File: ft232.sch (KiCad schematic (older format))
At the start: 18 parts, among them J1 USB_B, U7 FT232RL, U8 PS2911-1-F3-A, U9 PS2911-1-F3-A

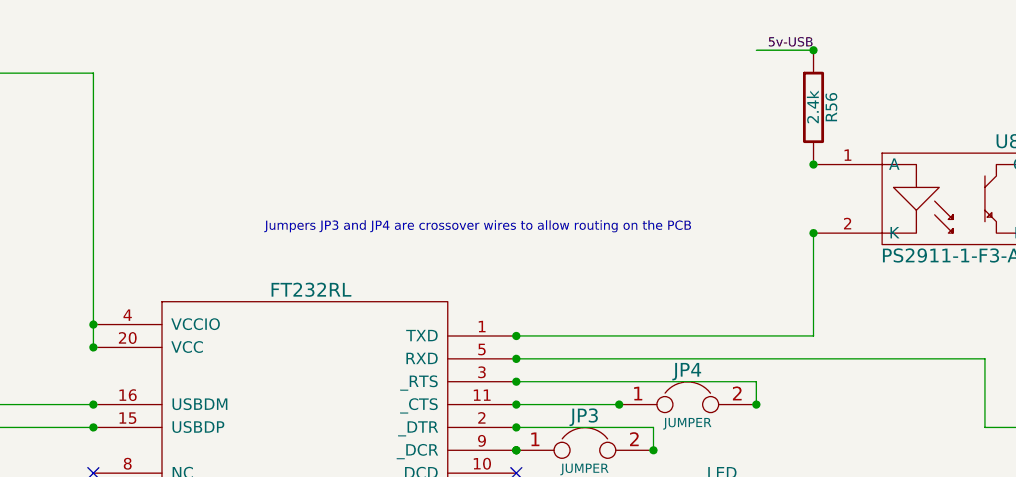
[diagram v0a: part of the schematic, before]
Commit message: Updated Schematics, PDF, BOM for 4cyl Sequential Injection
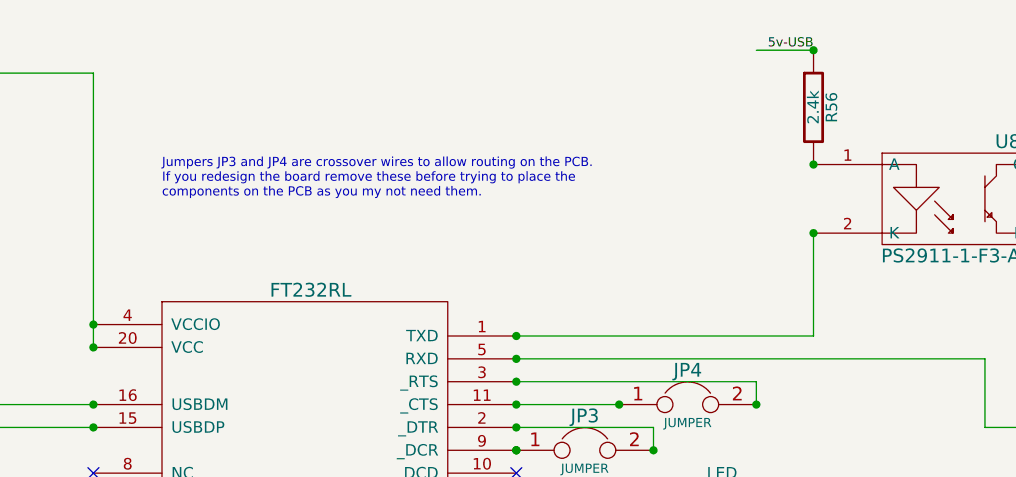
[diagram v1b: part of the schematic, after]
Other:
- note added: "Jumpers JP3 and JP4 are crossover wires to allow routing on the PCB.\nIf you redesign the board remove these before trying to place the \ncomponents on the PCB as you my not need them."
- note removed: "Jumpers JP3 and JP4 are crossover wires to allow routing on the PCB"
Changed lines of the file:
@@
-EESchema Schematic File Version 2  date Tue 24 Jan 2012 02:18:15 PM EST
+EESchema Schematic File Version 2  date Tue 24 Jan 2012 11:15:10 PM EST
 LIBS:power
 LIBS:device
@@
 Sheet 3 7
 Title "Jaguar PCB for FreeEMS"
-Date "24 jan 2012"
+Date "25 jan 2012"
 Rev "A.1"
 Comp "diyefi.org"
@@
 Text HLabel 9350 2500 2    40   Input ~ 0
 GND
-Text Notes 5700 2500 0    40   ~ 0
-Jumpers JP3 and JP4 are crossover wires to allow routing on the PCB
+Text Notes 5250 2350 0    40   ~ 0
+Jumpers JP3 and JP4 are crossover wires to allow routing on the PCB.\nIf you redesign the board remove these before trying to place the \ncomponents on the PCB as you my not need them.
 Wire Wire Line
 	9350 2600 9350 2500
